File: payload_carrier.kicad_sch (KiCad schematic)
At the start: 49 parts, among them J1 POWER IN, J2 USB_C_Receptacle_USB2.0_16P, J3 LEFT MikroBUS, J4 RIGHT MikroBUS, J5 Conn_01x05, J6 Micro_SD_Card, SW1 SW_Push, U1 TPS73733DCQR, U2 STM32G0B1CBTx, U3 TPS562202S, Y1 C7S-8.000-12-3030-X-R

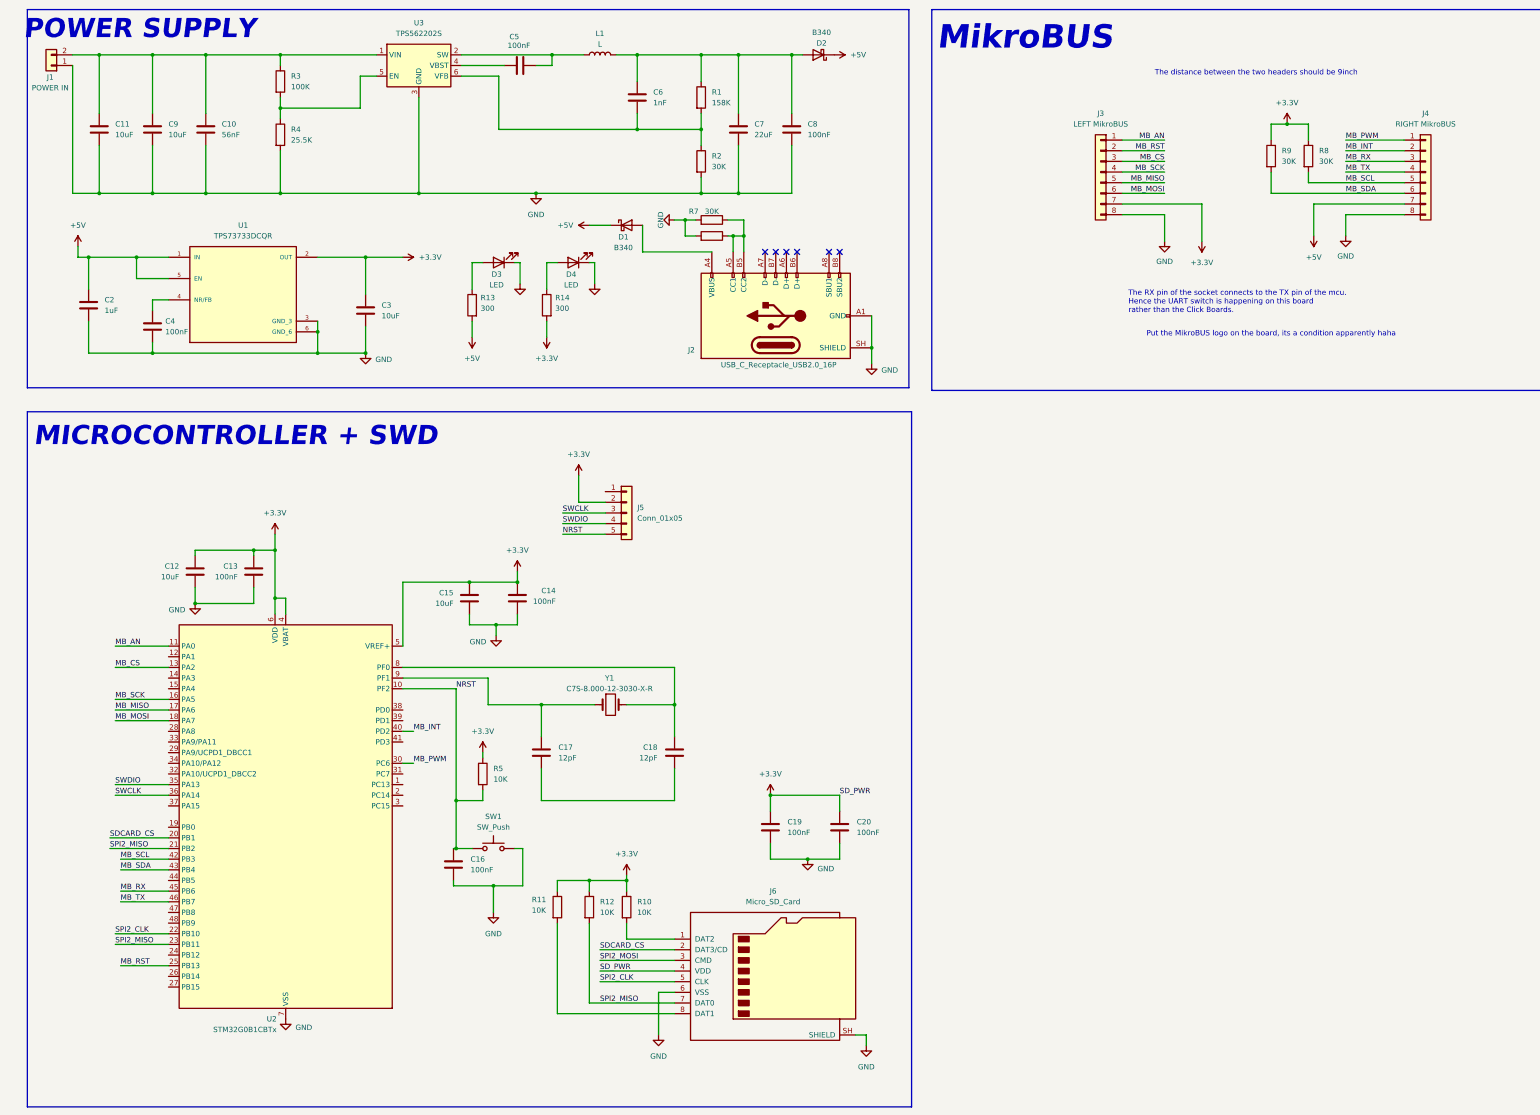
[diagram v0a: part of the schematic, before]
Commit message: Schematics removed, left block skeleton
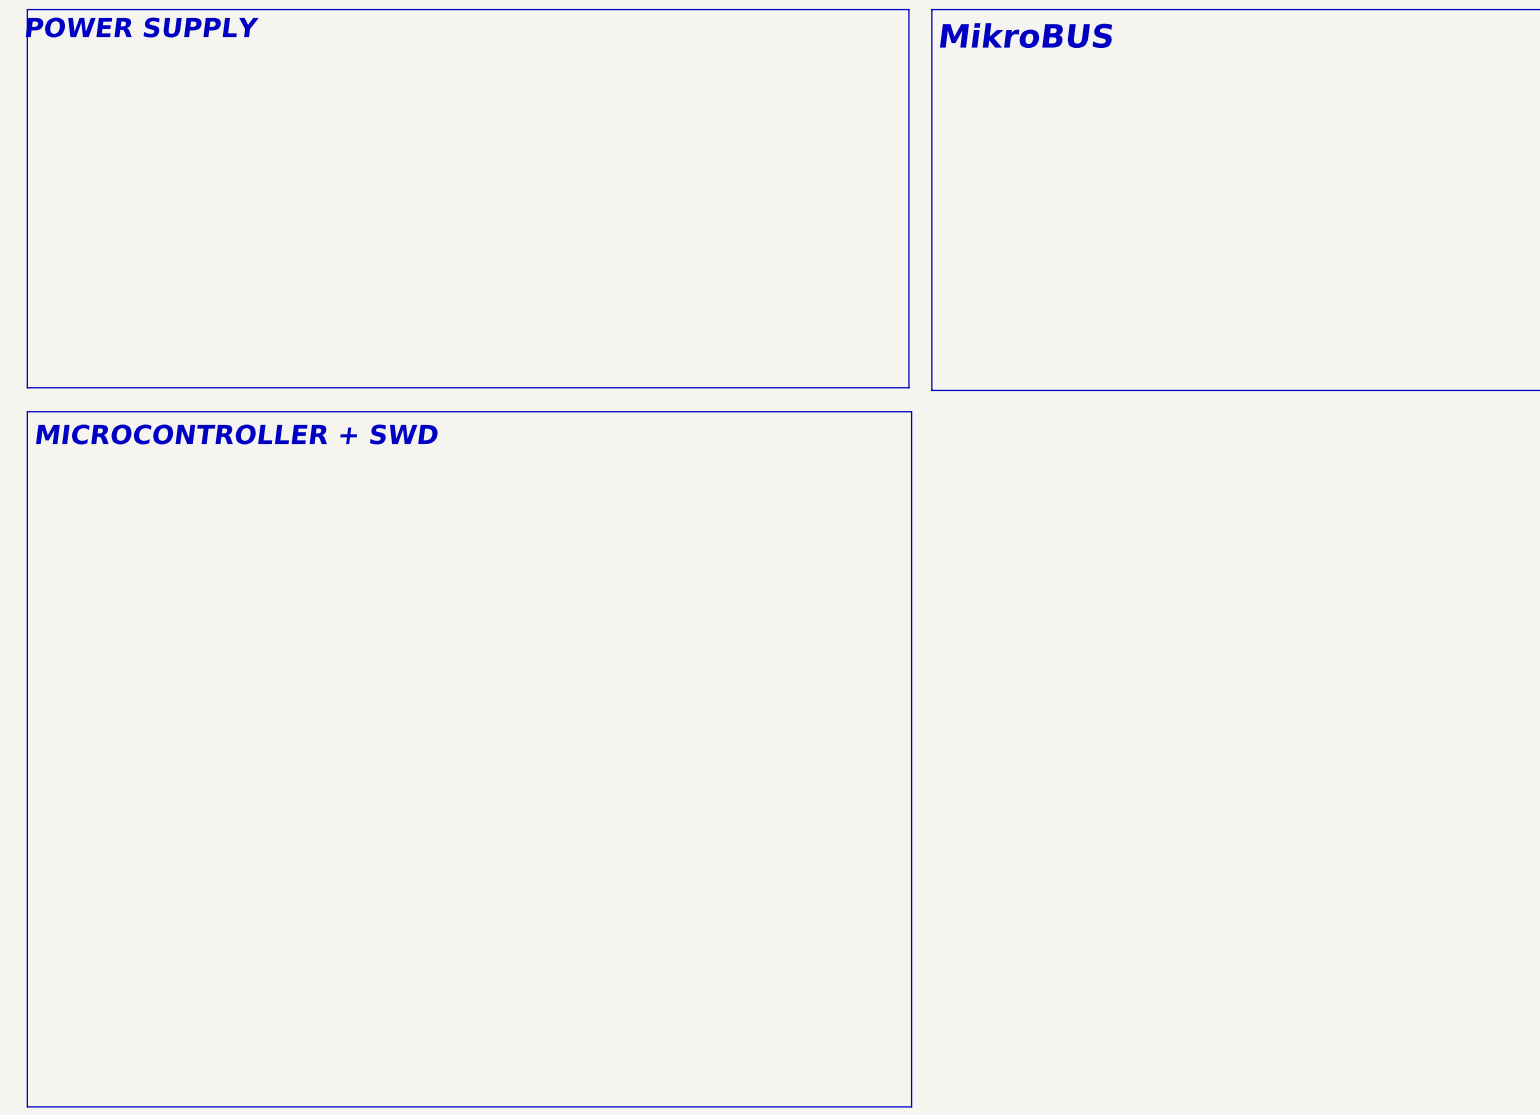
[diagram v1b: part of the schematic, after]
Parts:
- removed C10: 56nF, symbol KiCad:C
- removed C11, C12, C15, C3, C9: 10uF, symbol KiCad:C
- removed C13, C14, C4, C5, C8: 100nF, symbol KiCad:C
- removed C16, C19, C20: 100nF, Capacitor_SMD:C_0805_2012Metric_Pad1.18x1.45mm_HandSolder, symbol KiCad:C
- removed C17, C18: 12pF, Capacitor_SMD:C_0805_2012Metric_Pad1.18x1.45mm_HandSolder, symbol KiCad:C
- removed C2: 1uF, symbol KiCad:C
- removed C6: 1nF, symbol KiCad:C
- removed C7: 22uF, symbol KiCad:C
- removed D1, D2: B340, My FeetPics:DIOM5226X240N, symbol KiCad:B340
- removed D3, D4: LED, LED_SMD:LED_0805_2012Metric, symbol Device:LED
- removed J1: POWER IN, symbol KiCad:Conn_01x02
- removed J2: USB_C_Receptacle_USB2.0_16P, symbol KiCad:USB_C_Receptacle_USB2.0_16P
- removed J3: LEFT MikroBUS, symbol KiCad:Conn_01x08
- removed J4: RIGHT MikroBUS, symbol KiCad:Conn_01x08
- removed J5: Conn_01x05, Connector_PinHeader_2.54mm:PinHeader_1x05_P2.54mm_Vertical, symbol KiCad:Conn_01x05
- removed J6: Micro_SD_Card, symbol KiCad:Micro_SD_Card
- removed L1: L, symbol KiCad:L
- removed R1: 158K, symbol KiCad:R
- removed R10, R11, R12, R5: 10K, symbol KiCad:R
- removed R13, R14: 300, Resistor_SMD:R_0805_2012Metric_Pad1.20x1.40mm_HandSolder, symbol Device:R
- removed R2, R6, R7, R8, R9: 30K, symbol KiCad:R
- removed R3: 100K, symbol KiCad:R
- removed R4: 25.5K, symbol KiCad:R
- removed SW1: SW_Push, Button_Switch_SMD:SW_Push_1P1T_NO_E-Switch_TL3301NxxxxxG, symbol KiCad:SW_Push
- removed U1: TPS73733DCQR, TPS73733DCQR:IC_TPS73733DCQR, symbol My FeetPics:TPS73733DCQR
- removed U2: STM32G0B1CBTx, Package_QFP:LQFP-48_7x7mm_P0.5mm, symbol KiCad:STM32G0B1CBTx
- removed U3: TPS562202S, Package_TO_SOT_SMD:SOT-563, symbol KiCad:TPS562202S
- removed Y1: C7S-8.000-12-3030-X-R, Crystal:Crystal_SMD_7050-4Pin_7.0x5.0mm, symbol KiCad:Crystal
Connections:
- no-connect marks 6 -> 0
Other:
- note removed: "Put the MikroBUS logo on the board, its a condition apparently haha"
- note removed: "The RX pin of the socket connects to the TX pin of the mcu. Hence the UART switch is happening on this board rather than the Click Boards."
- note removed: "The distance between the two headers should be 9inch"

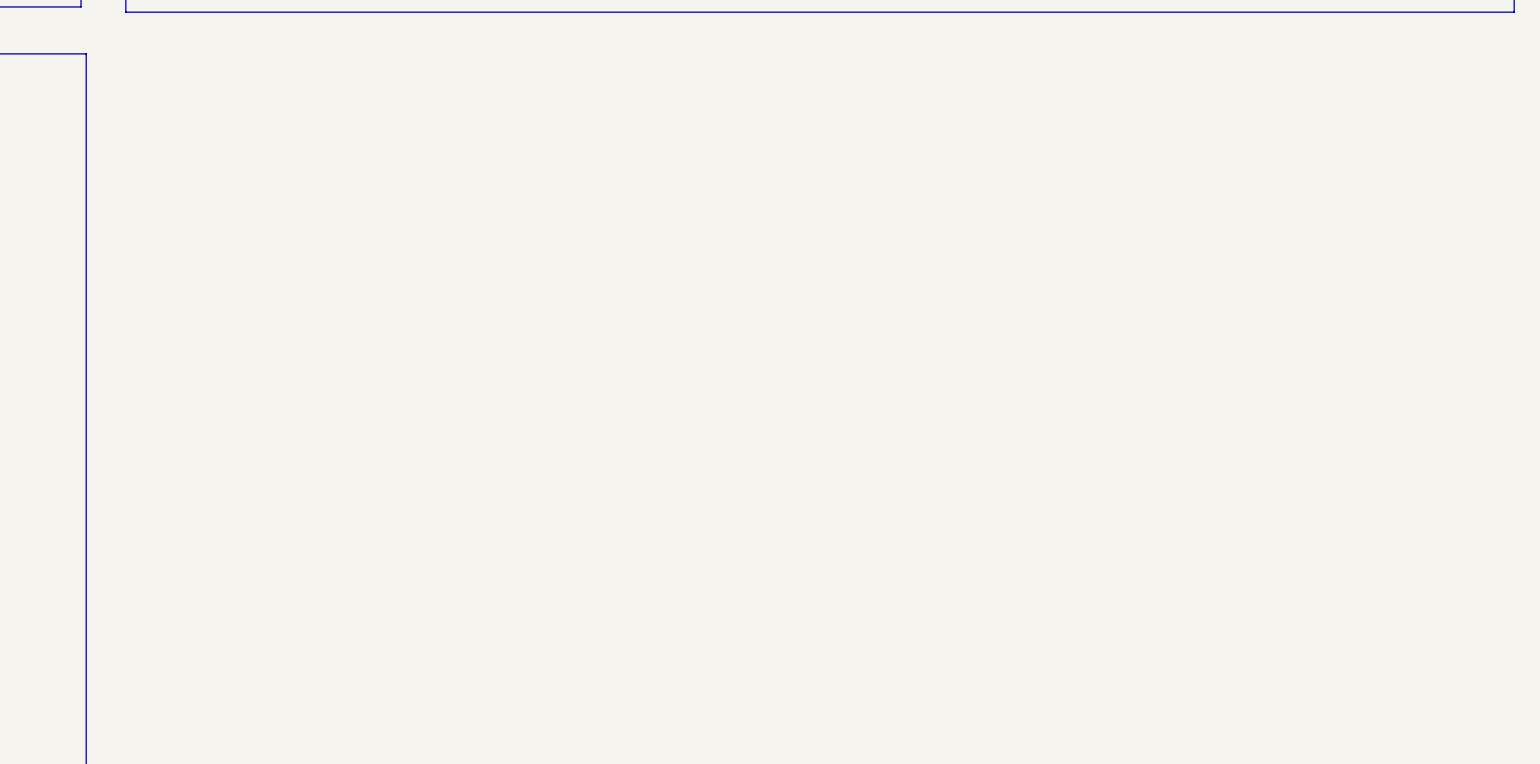
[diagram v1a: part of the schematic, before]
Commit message: Updated footprints and Library names
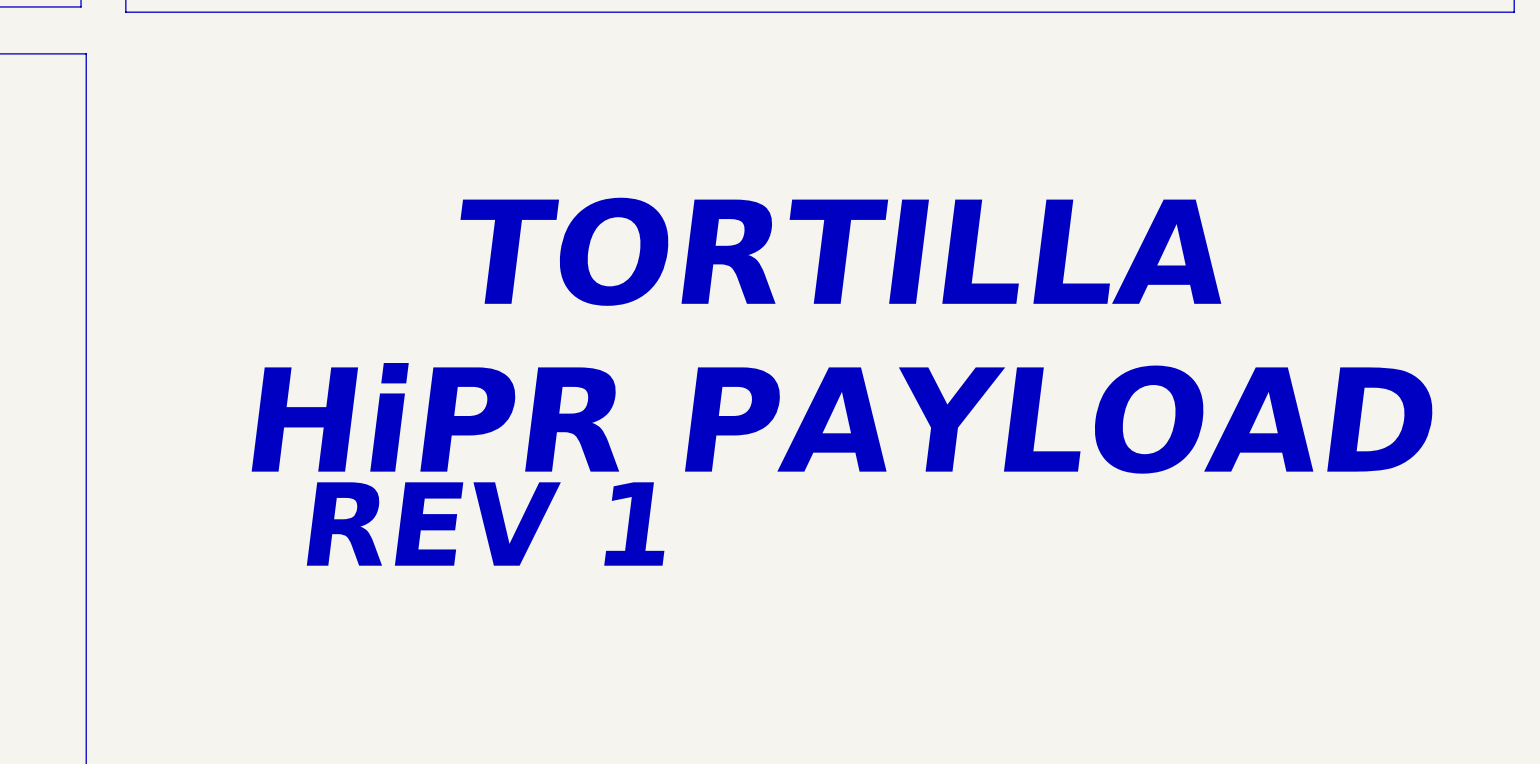
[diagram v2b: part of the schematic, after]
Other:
- note added: "REV 1"
- note added: "TORTILLA HiPR PAYLOAD"
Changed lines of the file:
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@@
+		)
+	)
+	(text "TORTILLA\nHiPR PAYLOAD"
+		(exclude_from_sim no)
+		(at 319.278 149.352 0)
+		(effects
+			(font
+				(face "JetBrainsMonoNL NF")
+				(size 12.7 12.7)
+				(thickness 1.524)
+				(bold yes)
+				(italic yes)
+				(color 0 0 0 1)
+			)
+		)
+	)
+	(text "REV 1"
+		(exclude_from_sim no)
+		(at 276.352 172.212 0)
+		(effects
+			(font
+				(size 10.16 10.16)
+				(thickness 0.254)
+				(bold yes)
+				(italic yes)
+			)
 		)
 	)

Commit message: schematics finished for layout session
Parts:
- added C1, C2: 1uF, symbol KiCad:C
- added C10, C14, C7, C9: 100nF, symbol KiCad:C
- added C11, C4, C5: 10uF, symbol KiCad:C
- added C12, C13: 12pF, symbol KiCad:C
- added C3: 10nF, symbol KiCad:C
- added C6: 56nF, symbol KiCad:C
- added C8: 22uF, symbol KiCad:C
- added D1, D2: B340, symbol KiCad:D
- added D3, D4: LED, symbol KiCad:LED
- added J1: Conn_01x02, symbol KiCad:Conn_01x02
- added J2: USB_C_Receptacle_USB2.0_16P, symbol KiCad:USB_C_Receptacle_USB2.0_16P
- added J3, J4: Conn_01x08, symbol KiCad:Conn_01x08
- added J5: Conn_01x05, symbol KiCad:Conn_01x05
- added J6: Micro_SD_Card, symbol KiCad:Micro_SD_Card
- added L1: 3.3uH, symbol KiCad:L
- added R1: 100K, symbol KiCad:R
- added R10, R9: 4.7K, symbol KiCad:R
- added R11, R12, R13, R14: 10K, symbol KiCad:R
- added R2: 25.5K, symbol KiCad:R
- added R3: 158K, symbol KiCad:R
- added R4: 30K, symbol KiCad:R
- added R5, R6: 5.1K, symbol KiCad:R
- added R7, R8: 300, symbol KiCad:R
- added SW1: SW_MEC_5G, symbol KiCad:SW_MEC_5G
- added U1: TPS73733DCQR, TPS73733DCQR:IC_TPS73733DCQR, symbol My Symbols:TPS73733DCQR
- added U2: TPS562242DRLR, Package_TO_SOT_SMD:SOT-563, symbol KiCad:TPS562202
- added U3: STM32G0B1CBTx, Package_QFP:LQFP-48_7x7mm_P0.5mm, symbol KiCad:STM32G0B1CBTx
- added Y1: Crystal, symbol KiCad:Crystal
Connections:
- new net: C7.1, U2.4 (VBST)
- new net: C7.2, L1.1, U2.2 (SW)
- new net: R1.2, R2.1, U2.5 (EN)
- new net: C4.1, C5.1, C6.1, J1.1 (Pin_1), R1.1, U2.1 (VIN)
- new net: D3.2 (A), R7.1
- new net: D2.2 (A), J2.A4 (VBUS), J2.A9 (VBUS), J2.B4 (VBUS), J2.B9 (VBUS)
- new net: C12.1, U3.9 (PF1), Y1.1
- new net: C13.1, U3.8 (PF0), Y1.2
- new net: C8.1, C9.1, D1.2 (A), L1.2, R3.1
- new net: R3.2, R4.1, U2.6 (VFB)
- new net: J6.8 (DAT1), R14.2
- new net: J2.A5 (CC1), R6.2
- new net: C3.1, U1.4 (NR/FB)
- new net: J2.B5 (CC2), R5.2
- new net: D4.2 (A), R8.1
- new net: J6.1 (DAT2), R12.2
- new net +3.3V: C10.1, C11.1, C2.1, J3.7 (Pin_7), J5.2 (Pin_2), J6.4 (VDD), R10.1, R11.1, R12.1, R13.1, R14.1, R7.2, R9.1, U1.2 (OUT), U3.4 (VBAT), U3.6 (VDD)
- new net +5V: C1.1, D1.1 (K), D2.1 (K), J4.7 (Pin_7), R8.2, U1.1 (IN), U1.5 (EN)
- new net GND: C1.2, C10.2, C11.2, C12.2, C13.2, C14.2, C2.2, C3.2, C4.2, C5.2, C6.2, C8.2, C9.2, D3.1 (K), D4.1 (K), J1.2 (Pin_2), J2.A1 (GND), J2.A12 (GND), J2.B1 (GND), J2.B12 (GND), J2.SH (SHIELD), J3.8 (Pin_8), J4.8 (Pin_8), J5.1 (Pin_1), J6.6 (VSS), J6.SH (SHIELD), R2.2, R4.2, R5.1, R6.1, SW1.3 (B), SW1.4 (B), U1.3 (GND_3), U1.6 (GND_6), U2.3 (GND), U3.7 (VSS)
- new net MB_AN: J3.1 (Pin_1), U3.11 (PA0)
- new net MB_CS: J3.3 (Pin_3), U3.13 (PA2)
- new net MB_INT: J4.2 (Pin_2), U3.40 (PD2)
- new net MB_MISO: J3.5 (Pin_5), U3.17 (PA6)
- new net MB_MOSI: J3.6 (Pin_6), U3.18 (PA7)
- new net MB_PWM: J4.1 (Pin_1), U3.30 (PC6)
- new net MB_RST: J3.2 (Pin_2), U3.25 (PB13)
- new net MB_RX: J4.3 (Pin_3), U3.45 (PB6)
- new net MB_SCK: J3.4 (Pin_4), U3.16 (PA5)
- new net MB_SCL: J4.5 (Pin_5), R10.2, U3.42 (PB3)
- new net MB_SDA: J4.6 (Pin_6), R9.2
- new net MB_SDL: U3.43 (PB4)
- new net MB_TX: J4.4 (Pin_4), U3.46 (PB7)
- new net NRST: C14.1, J5.5 (Pin_5), R11.2, SW1.1 (A), SW1.2 (A), U3.10 (PF2)
- new net SD_CLK: U3.22 (PB10)
- new net SD_CS: J6.2 (DAT3/CD), U3.20 (PB1)
- new net SD_MISO: J6.7 (DAT0), R13.2, U3.21 (PB2)
- new net SD_MOSI: J6.3 (CMD), U3.23 (PB11)
- new net SD_SCK: J6.5 (CLK)
- new net SWDCLK: J5.3 (Pin_3), U3.36 (PA14)
- new net SWDIO: J5.4 (Pin_4), U3.37 (PA15)
- no-connect marks 0 -> 6
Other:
- note added: "8MHz"
